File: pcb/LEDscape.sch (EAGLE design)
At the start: 41 parts, among them IC1 MAX3041CUE, IC2 MAX3041CUE, IC3 MAX3041CUE, IC4 MAX3041CUE, IC5 MAX3041CUE, IC6 MAX3041CUE, IC7 MAX3041CUE, IC8 MAX3041CUE

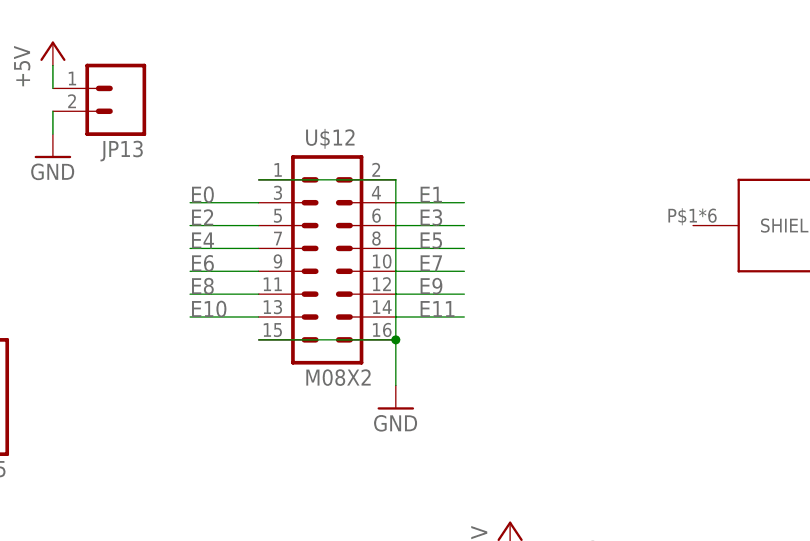
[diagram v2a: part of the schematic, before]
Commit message: Updated BBB footprint, mounting holes in LEDscape baord, small cleanups
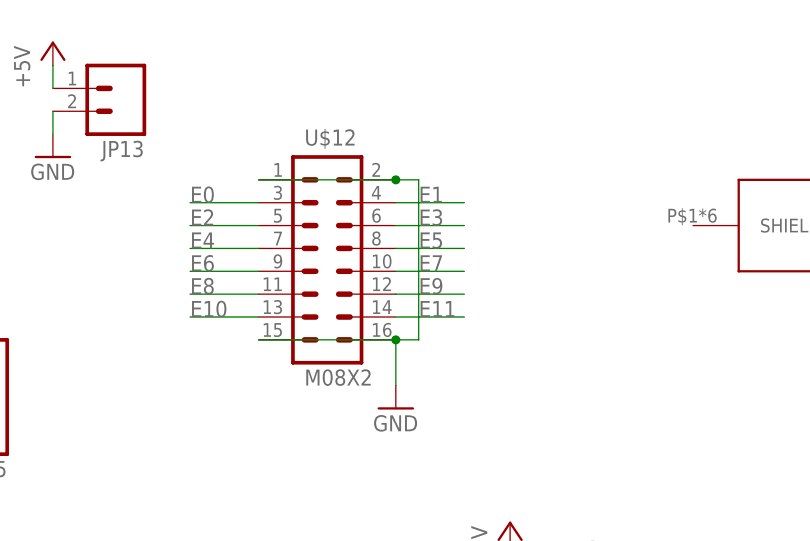
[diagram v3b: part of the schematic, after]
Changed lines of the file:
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@@
 <pinref part="U$12" gate="G$1" pin="2"/>
 <wire x1="76.2" y1="139.7" x2="91.44" y2="139.7" width="0.1524" layer="91"/>
-<wire x1="91.44" y1="139.7" x2="91.44" y2="121.92" width="0.1524" layer="91"/>
+<wire x1="91.44" y1="139.7" x2="93.98" y2="139.7" width="0.1524" layer="91"/>
+<wire x1="93.98" y1="139.7" x2="93.98" y2="121.92" width="0.1524" layer="91"/>
+<wire x1="93.98" y1="121.92" x2="91.44" y2="121.92" width="0.1524" layer="91"/>
+<junction x="91.44" y="139.7"/>
 </segment>
 <segment>
